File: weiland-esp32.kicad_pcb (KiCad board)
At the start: 2 copper layers, 20.2 x 58 mm, 22 parts, among them J1 S02B-PASK-2, J2 20021221-00006T4LF, J3 S02B-PASK-2, J4 S02B-PASK-2, J6 S02B-PASK-2, J7 S02B-PASK-2, U1 ESP32-WROOM-32E(8MB), U2 AMS1117-3.3_C347222, U3 GR6205-SOP-8, U4 MAX98357AEWL_T

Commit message: good schematic before unshrouded header
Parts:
- removed J3, J4: S02B-PASK-2, footprints:CONN2_S02B-PASK-2_JST
- removed U3: GR6205-SOP-8, motor_driver:SOP127P780X200-8N
- added P1: S04B-PASK-2_LF__SN_, S04B-PASK-2_LF__SN_:JST_S04B-PASK-2, F.Cu at (138.4, 99.9)
- added P2: S04B-PASK-2_LF__SN_, S04B-PASK-2_LF__SN_:JST_S04B-PASK-2, F.Cu at (172.8, 93.5)
- added U5: ULN2003F12FN-7, ULN2003:U-DFN3030-10_DIO, F.Cu at (171.5, 101.4)
- C1: footprint 22uF capacitor:CAPC1608X90N -> 100ohm-resistor:RESC1005X40N
- C4, C5: value 10uF -> 22uF; footprint 10 uF capacitor:CAPC1608X90N -> 100ohm-resistor:RESC1005X40N
- C6: footprint 10 uF capacitor:CAPC1608X90N -> 100ohm-resistor:RESC1005X40N
- C7, C8: footprint 220pF capacitor:CAPC1005X55N -> 100ohm-resistor:RESC1005X40N
- R1: value 5.1kΩ -> 100Ω; footprint 5-1-ohm-resistor:RES_ERJ2RKF5101X -> 100ohm-resistor:RESC1005X40N
- U4: footprint MAX98357AEWL_T:BGA9N40P3X3_134X143X69N -> MAX98357AETE_T:QFN50P300X300X80-17N
- moved J7 42.5 mm to (173.0, 108.1), turned to -90 degrees
- moved J2 33.5 mm to (177.4, 102.2), turned to 0 degrees
- moved J6 28.1 mm to (138.4, 92.3), turned to 90 degrees
- moved C3 27.8 mm to (172.5, 105.1), turned to 0 degrees
- moved U1 24.0 mm to (159.1, 96.1), turned to 0 degrees
- moved C5 22.7 mm to (147.6, 99.8)
- moved C4 21.1 mm to (144.1, 99.8), turned to 180 degrees
- moved U2 20.2 mm to (145.7, 94.6), turned to -90 degrees
- moved C2 20.2 mm to (146.5, 89.5)
- moved C1 20.0 mm to (143.8, 89.5)
- moved R1 17.0 mm to (147.9, 101.3), turned to 0 degrees
- moved LED1 13.6 mm to (145.1, 101.4), turned to 180 degrees
- moved J1 12.3 mm to (138.4, 109.4), turned to 90 degrees
- moved C6 10.8 mm to (143.3, 104.1), turned to -90 degrees
- moved U4 7.80 mm to (146.7, 104.8)
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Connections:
- U1 pad 10: /IO25 -> unconnected-(U1-IO25-Pad10)
- U1 pad 11: /IO26 -> unconnected-(U1-IO26-Pad11)
- U1 pad 12: /IO27 -> unconnected-(U1-IO27-Pad12)
- U1 pad 13: unconnected-(U1-IO14-Pad13) -> /IO14
- U1 pad 23: unconnected-(U1-IO15-Pad23) -> /IO15
- U1 pad 27: unconnected-(U1-IO16-Pad27) -> /IO16
- U1 pad 28: unconnected-(U1-IO17-Pad28) -> /IO17
- U1 pad 30: unconnected-(U1-IO18-Pad30) -> /IO18
- U1 pad 31: unconnected-(U1-IO19-Pad31) -> /IO19
- U1 pad 36: unconnected-(U1-IO22-Pad36) -> /IO22
- U1 pad 8: /IO32 -> unconnected-(U1-IO32-Pad8)
- U1 pad 9: /IO33 -> unconnected-(U1-IO33-Pad9)
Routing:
- net GND: track 104.8 -> 1.40 mm, vias 4 -> 2
- net /OUTN: track 46.2 -> 0.00 mm, vias 6 -> 0
- net /OUTP: track 44.6 -> 0.00 mm, vias 2 -> 0
- net /RXD0: track 32.6 -> 0.00 mm, vias 2 -> 0
- net /TXD0: track 32.5 -> 0.00 mm, vias 2 -> 0
- net +5V: track 32.4 -> 62.2 mm, vias 2 -> 1
- net /IO0: track 26.6 -> 0.00 mm, vias 2 -> 0
- net /OUTA: track 31.6 -> 7.37 mm
- net /EN: track 22.5 -> 0.00 mm, vias 2 -> 0
- net /IO25: track 20.6 -> 0.00 mm
- net /IO26: track 13.1 -> 0.00 mm, vias 2 -> 0
- net /IO27: track 13.0 -> 0.00 mm, vias 2 -> 0
- net +3V3: track 21.4 -> 13.7 mm, vias 2 -> 0
- net Net-(U4-OUTN): track 3.06 -> 0.00 mm
- net /IO33: track 2.58 -> 0.00 mm
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- added copper zone on B.Cu, net GND
- added copper zone on F.Cu, net GND
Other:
- board size 20.2 x 58 mm -> 51.5 x 24.2 mm

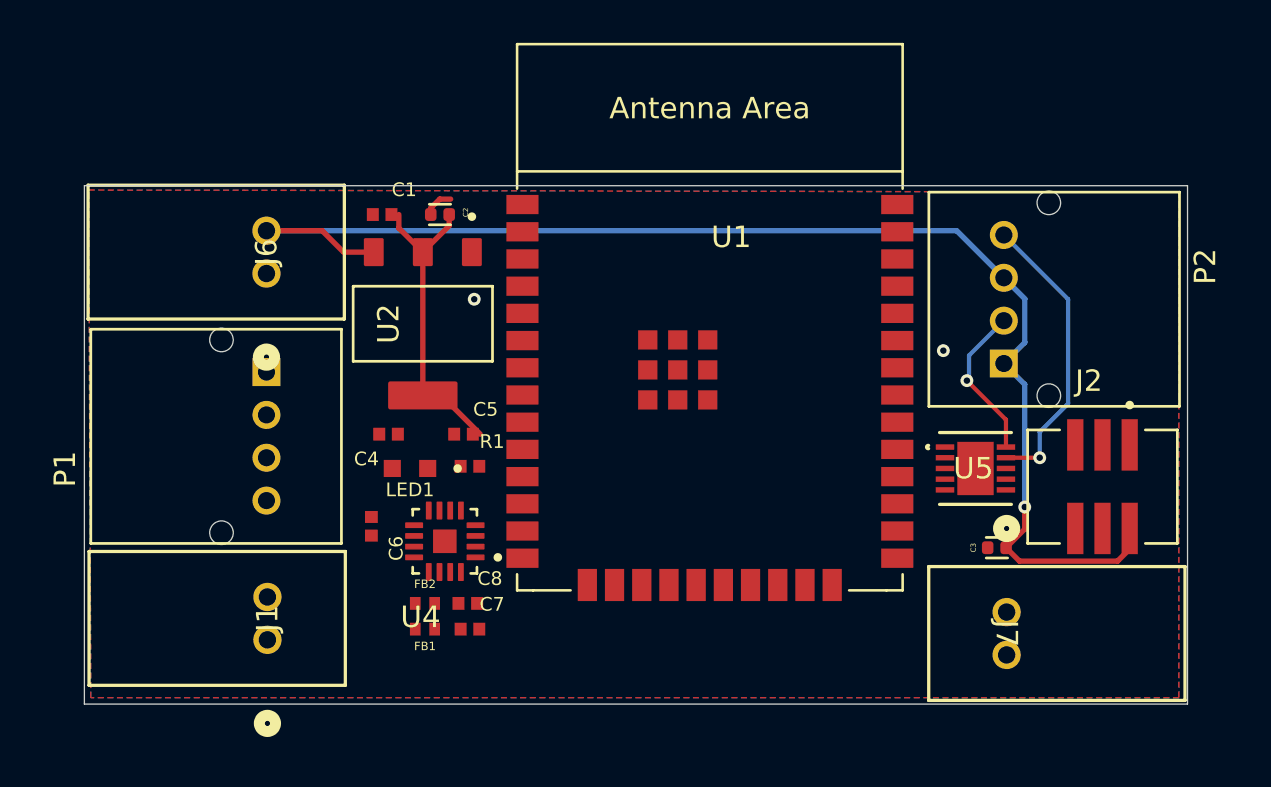
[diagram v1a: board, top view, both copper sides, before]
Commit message: test point schematic, before adding to layout
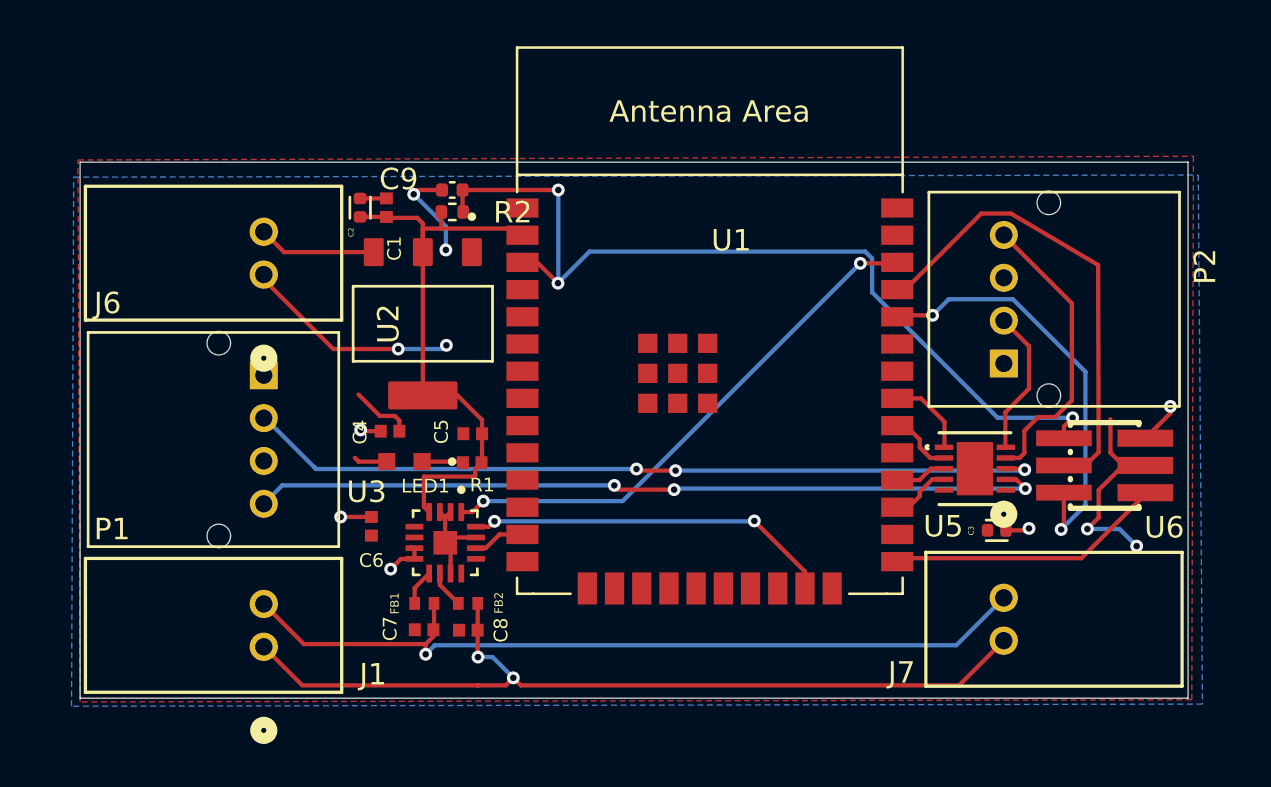
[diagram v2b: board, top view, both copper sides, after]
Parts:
- removed J2: 20021221-00006T4LF, dc3-6p:dc3-6p
- removed U4: MAX98357AEWL_T, MAX98357AETE_T:QFN50P300X300X80-17N
- added C9: 0.1uF, Capacitor_SMD:C_0402_1005Metric, F.Cu at (147.1, 88.4)
- added R2: 10k, Resistor_SMD:R_0402_1005Metric, F.Cu at (147.1, 89.4)
- added U3: MAX98357AETE_T, MAX98357AETE_T:QFN50P300X300X80-17N, F.Cu at (146.7, 104.9)
- added U6: DZ127S-22-06-55, unshroudedheader:HDR-SMD_6P-P1.27-V-M-R2-C3-S1.27-LS5.5-1, F.Cu at (177.5, 101.3)
- moved C2 3.74 mm to (142.8, 89.2), turned to -90 degrees
- moved C7 2.14 mm to (145.8, 108.9), turned to 180 degrees
- moved FB2 2.01 mm to (147.8, 107.7)
- moved C8 1.25 mm to (147.8, 109.0), turned to 180 degrees
- moved FB1 1.20 mm to (145.8, 107.7)
- moved C3 0.81 mm to (172.5, 104.3)
- moved J7 0.68 mm to (172.8, 107.4)
- moved C5 0.43 mm to (148.0, 99.8)
- moved LED1 0.41 mm to (144.8, 101.1)
- moved C1 0.38 mm to (144.0, 89.2), turned to -90 degrees
- moved J1 0.37 mm to (138.3, 109.7)
- moved R1 0.20 mm to (148.0, 101.1)
- moved P1 0.20 mm to (138.3, 100.0)
- moved U1 0.16 mm to (159.1, 96.2)
- moved C4 0.16 mm to (144.2, 99.7)
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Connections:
- net +3V3 renamed +3.3V
- J1 pad 1: /OUTP -> /OUTN
- J1 pad 2: /OUTN -> /OUTP
- P1 pad 2: /OUTD -> /OUTC
- P1 pad 4: /OUTC -> /OUTD
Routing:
- net +5V: track 62.2 -> 12.9 mm, vias 1 -> 5
- net /EN: track 0.00 -> 41.8 mm, vias 0 -> 3
- net /OUTN: track 0.00 -> 41.1 mm, vias 0 -> 2
- net /OUTP: track 0.00 -> 38.9 mm, vias 0 -> 1
- net /OUTC: track 0.00 -> 37.5 mm, vias 0 -> 3
- net /OUTD: track 0.00 -> 37.1 mm, vias 0 -> 3
- net GND: track 1.40 -> 35.2 mm, vias 2 -> 6
- net /IO22: track 0.00 -> 25.2 mm, vias 0 -> 2
- net /TXD0: track 0.00 -> 22.1 mm
- net /RXD0: track 0.00 -> 20.1 mm, vias 0 -> 2
- net /IO15: track 0.00 -> 17.2 mm, vias 0 -> 2
- net +3.3V: track 13.7 -> 28.0 mm
- net /IO0: track 0.00 -> 13.0 mm
- net /IO19: track 0.00 -> 3.84 mm
- net /IO18: track 0.00 -> 3.04 mm
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- added copper zone on B.Cu, net +5V
- removed copper zone on B.Cu, net GND
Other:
- board size 51.5 x 24.2 mm -> 51.7 x 25 mm

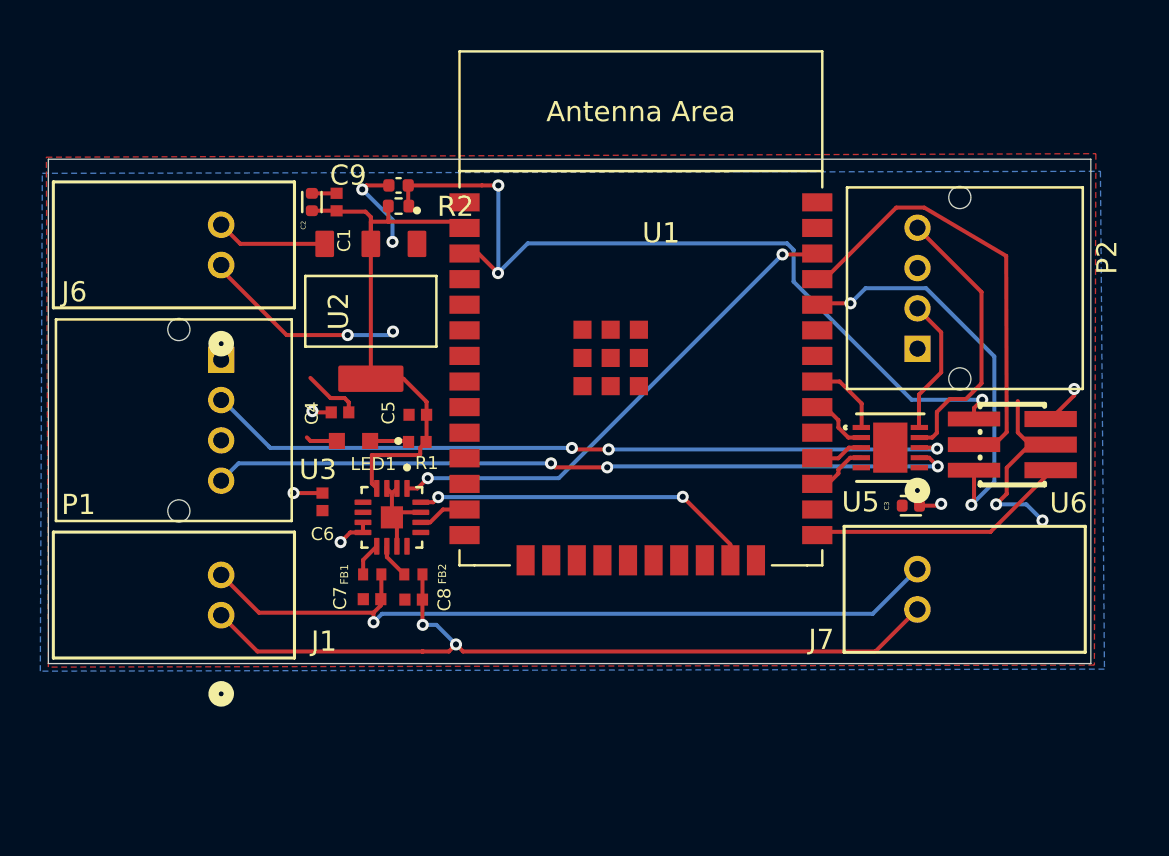
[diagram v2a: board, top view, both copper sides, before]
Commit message: 52x39 board w/ holes
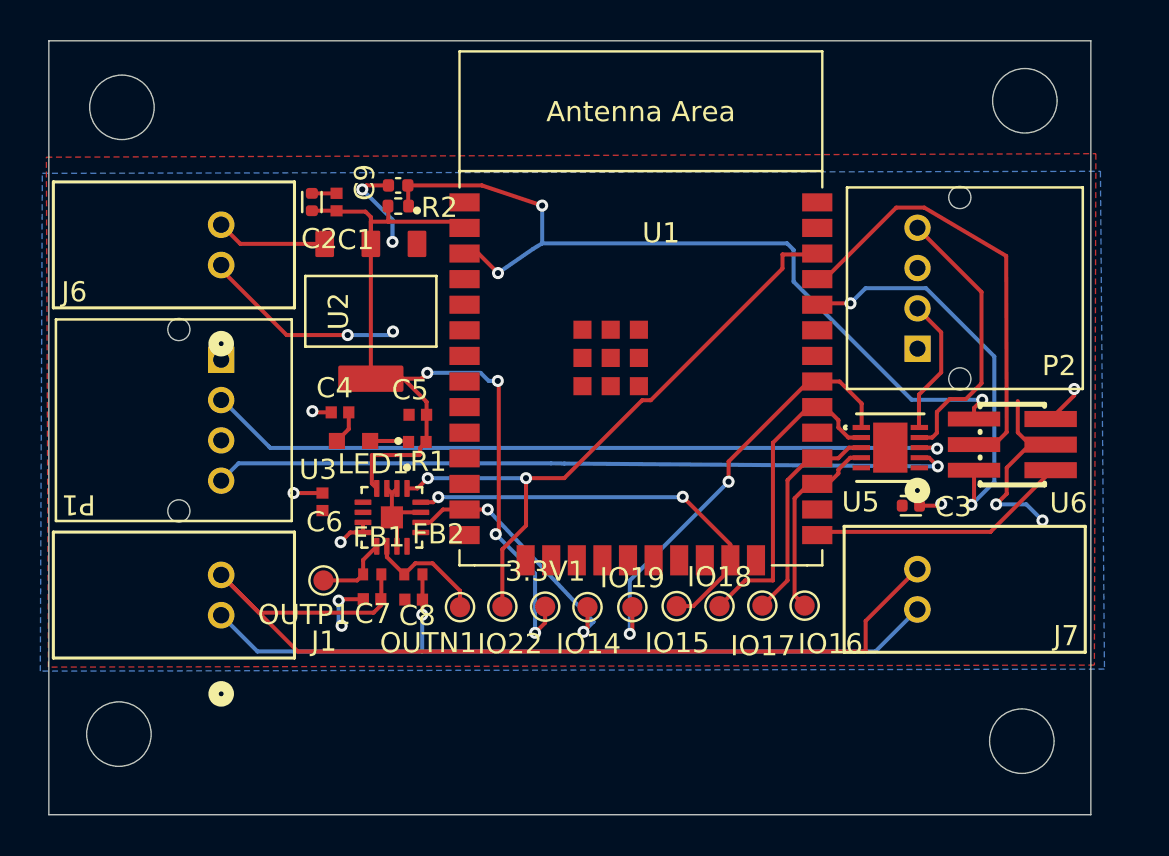
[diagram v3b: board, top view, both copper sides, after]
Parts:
- added 3.3V1: TestPoint, TestPoint:TestPoint_Pad_D1.0mm, F.Cu at (154.3, 109.3)
- added IO14: TestPoint, TestPoint:TestPoint_Pad_D1.0mm, F.Cu at (156.4, 109.3)
- added IO15: TestPoint, TestPoint:TestPoint_Pad_D1.0mm, F.Cu at (160.9, 109.3)
- added IO16: TestPoint, TestPoint:TestPoint_Pad_D1.0mm, F.Cu at (167.2, 109.2)
- added IO17: TestPoint, TestPoint:TestPoint_Pad_D1.0mm, F.Cu at (165.1, 109.2)
- added IO18: TestPoint, TestPoint:TestPoint_Pad_D1.0mm, F.Cu at (163.0, 109.3)
- added IO19: TestPoint, TestPoint:TestPoint_Pad_D1.0mm, F.Cu at (158.7, 109.3)
- added IO22: TestPoint, TestPoint:TestPoint_Pad_D1.0mm, F.Cu at (152.2, 109.3)
- added OUTN1: TestPoint, TestPoint:TestPoint_Pad_D1.0mm, F.Cu at (150.1, 109.3)
- added OUTP1: TestPoint, TestPoint:TestPoint_Pad_D1.0mm, F.Cu at (143.3, 108.0)
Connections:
- net Net-(U3-OUTN) renamed /PRE-OUTN
- net Net-(U3-OUTP) renamed /PRE-OUTP
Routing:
- net +3.3V: track 28.0 -> 49.5 mm, vias 0 -> 4
- net /IO19: track 3.84 -> 21.8 mm, vias 0 -> 2
- net /IO18: track 3.04 -> 16.0 mm
- net /IO14: track 2.44 -> 13.3 mm, vias 0 -> 2
- net /OUTP: track 38.9 -> 49.1 mm, vias 1 -> 0
- net /IO17: track 2.42 -> 11.1 mm
- net /IO22: track 25.2 -> 32.5 mm
- net /IO16: track 2.85 -> 9.81 mm
- net /PRE-OUTN: track 1.75 -> 6.12 mm
- net /IO15: track 17.2 -> 21.1 mm
- net /PRE-OUTP: track 1.68 -> 3.77 mm
- net /OUTN: track 41.1 -> 40.0 mm, vias 2 -> 1
- net GND: track 35.2 -> 34.9 mm, vias 6 -> 8
- net /OUTD: track 37.1 -> 37.0 mm, vias 3 -> 1
- net /OUTC: vias 3 -> 1
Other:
- board size 51.7 x 25 mm -> 51.7 x 38.4 mm

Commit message: before deleting all traces
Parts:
- added H1: MountingHole, MountingHole:MountingHole_3.2mm_M3, F.Cu at (137.7, 108.3)
- added H2: MountingHole, MountingHole:MountingHole_3.2mm_M3, F.Cu at (175.0, 119.1)
- moved J1 8.60 mm to (129.7, 109.6)
- moved J6 8.60 mm to (129.7, 92.2)
- moved P1 8.60 mm to (129.7, 100.0)
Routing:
- net /OUTP: track 49.1 -> 67.4 mm
- net +5V: track 12.9 -> 21.6 mm
- net /OUTN: track 40.0 -> 48.6 mm
- net /OUTC: track 37.5 -> 46.1 mm
- net /OUTD: track 37.0 -> 45.6 mm
- net GND: track 34.9 -> 43.5 mm
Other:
- board size 51.7 x 38.4 mm -> 70.8 x 24.6 mm

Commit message: board complete
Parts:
- added H3: MountingHole, MountingHole:MountingHole_3.2mm_M3, F.Cu at (172.4, 108.4)
- added H4: MountingHole, MountingHole:MountingHole_3.2mm_M3, F.Cu at (145.7, 91.4)
- moved P+1 33.1 mm to (174.7, 97.4)
- moved C9 30.1 mm to (177.1, 90.5)
- moved R2 30.1 mm to (177.1, 91.5)
- moved FB1 29.4 mm to (173.9, 99.4), turned to -90 degrees
- moved C7 28.9 mm to (174.2, 104.1), turned to -90 degrees
- moved FB2 28.5 mm to (175.1, 99.4), turned to -90 degrees
- moved C6 28.4 mm to (171.3, 99.7), turned to 180 degrees
- moved N1 28.2 mm to (174.7, 95.3)
- moved C8 28.0 mm to (175.4, 104.1), turned to -90 degrees
- moved H2 27.9 mm to (172.4, 91.3)
- moved U3 25.6 mm to (171.1, 97.0), turned to 0 degrees
- moved C3 19.0 mm to (185.9, 90.8), turned to 90 degrees
- moved C2 16.2 mm to (142.8, 105.4), turned to 90 degrees
- moved I22 14.3 mm to (166.5, 109.2)
- moved U6 10.7 mm to (182.0, 91.6)
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- renumbered IO14 to I14, IO15 to I15, IO16 to I16, IO17 to I17, IO18 to I18, IO19 to I19, IO22 to I22, OUTN1 to N1, OUTP1 to P+1, 3.3V1 to V3
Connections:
- P2 pad 2: /OUTA -> /OUTB
- P2 pad 4: /OUTB -> /OUTA
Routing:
- net +3.3V: track 49.5 -> 83.5 mm, vias 4 -> 8
- net GND: track 43.5 -> 22.3 mm, vias 8 -> 4
- net /IO14: track 13.3 -> 34.1 mm
- net /IO0: track 13.0 -> 27.0 mm, vias 0 -> 2
- net Net-(LED1-A): track 1.93 -> 14.0 mm
- net /OUTP: track 67.4 -> 56.8 mm, vias 0 -> 1
- net /OUTD: track 45.6 -> 36.5 mm
- net +5V: track 21.6 -> 12.7 mm, vias 5 -> 2
- net /TXD0: track 22.1 -> 13.5 mm, vias 0 -> 2
- net /OUTC: track 46.1 -> 37.6 mm
- net /EN: track 41.5 -> 33.4 mm, vias 3 -> 0
- net /OUTN: track 48.6 -> 56.0 mm
- net /RXD0: track 20.1 -> 12.9 mm
- net /OUTB: track 13.8 -> 7.35 mm, vias 0 -> 1
- net /IO17: track 11.1 -> 17.5 mm, vias 0 -> 4
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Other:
- board size 70.8 x 24.6 mm -> 58.5 x 24.2 mm

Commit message: test
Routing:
- removed copper zone on B.Cu, net +5V
- removed copper zone on F.Cu, net GND
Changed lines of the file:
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@@
 		)
 		(property "Value" "10uF"
-			(at 3.8768 1.0936 360)
+			(at 3.8768 1.0936 0)
 			(layer "F.Fab")
 			(effects
@@
 		)
 		(property "Footprint" "100ohm-resistor:RESC1005X40N"
-			(at 0 0 360)
+			(at 0 0 0)
 			(layer "F.Fab")
 			(hide yes)
@@
 		)
 		(property "Datasheet" ""
-			(at 0 0 360)
+			(at 0 0 0)
 			(layer "F.Fab")
 			(hide yes)
@@
 		)
 		(property "Description" "Unpolarized capacitor"
-			(at 0 0 360)
+			(at 0 0 0)
 			(layer "F.Fab")
 			(hide yes)
@@
 		)
 		(property "Value" "22uF"
-			(at 3.8768 1.0936 360)
+			(at 3.8768 1.0936 0)
 			(layer "F.Fab")
 			(effects
@@
 		)
 		(property "Footprint" "100ohm-resistor:RESC1005X40N"
-			(at 0 0 360)
+			(at 0 0 0)
 			(layer "F.Fab")
 			(hide yes)
@@
 		)
 		(property "Datasheet" ""
-			(at 0 0 360)
+			(at 0 0 0)
 			(layer "F.Fab")
 			(hide yes)
@@
 		)
 		(property "Description" ""
-			(at 0 0 360)
+			(at 0 0 0)
 			(layer "F.Fab")
 			(hide yes)
@@
 		)
 		(property "LCSC" "C22367823"
-			(at 0 0 360)
+			(at 0 0 0)
 			(layer "F.SilkS")
 			(hide yes)
@@
 		)
 		(property "Value" "0.1uF"
-			(at 0 1.16 360)
+			(at 0 1.16 0)
 			(layer "F.Fab")
 			(effects
@@
 		)
 		(fp_text user "${REFERENCE}"
-			(at 0 0 360)
+			(at 0 0 0)
 			(layer "F.Fab")
 			(effects
@@
 		)
 		(property "Value" "22uF"
-			(at 3.8768 1.0936 360)
+			(at 3.8768 1.0936 0)
 			(layer "F.Fab")
 			(effects
@@
 		)
 		(property "Footprint" "100ohm-resistor:RESC1005X40N"
-			(at 0 0 360)
+			(at 0 0 0)
 			(layer "F.Fab")
 			(hide yes)
@@
 		)
 		(property "Datasheet" ""
-			(at 0 0 360)
+			(at 0 0 0)
 			(layer "F.Fab")
 			(hide yes)
@@
 		)
 		(property "Description" ""
-			(at 0 0 360)
+			(at 0 0 0)
 			(layer "F.Fab")
 			(hide yes)
@@
 		)
 		(property "LCSC" "C22367823"
-			(at 0 0 360)
+			(at 0 0 0)
 			(layer "F.SilkS")
 			(hide yes)
@@
 		)
 		(property "Value" "10k"
-			(at 0 1.17 360)
+			(at 0 1.17 0)
 			(layer "F.Fab")
 			(effects
@@
 		)
 		(fp_text user "${REFERENCE}"
-			(at 0 0 360)
+			(at 0 0 0)
 			(layer "F.Fab")
 			(effects
@@
 		)
 		(property "Value" "MAX98357AETE_T"
-			(at 10.36 3.74 360)
+			(at 10.36 3.74 0)
 			(layer "F.Fab")
 			(effects
@@
 		)
 		(property "Footprint" "MAX98357AETE_T:QFN50P300X300X80-17N"
-			(at 0 0 360)
+			(at 0 0 0)
 			(layer "F.Fab")
 			(hide yes)
@@
 		)
 		(property "Datasheet" ""
-			(at 0 0 360)
+			(at 0 0 0)
 			(layer "F.Fab")
 			(hide yes)
@@
 		)
 		(property "Description" ""
-			(at 0 0 360)
+			(at 0 0 0)
 			(layer "F.Fab")
 			(hide yes)
@@
 		(net 47)
 	)
-	(zone
-		(net 1)
-		(net_name "GND")
-		(layer "F.Cu")
-		(hatch edge 0.5)
-		(connect_pads
-			(clearance 0.2)
-		)
-		(min_thickness 0.25)
-		(filled_areas_thickness no)
-		(fill yes
-			(thermal_gap 0.5)
-			(thermal_bridge_width 0.5)
-		)
-		(polygon
-			(pts
-				(xy 129.5 87.5) (xy 188.6 87.6) (xy 188.85 113.075) (xy 128.775 113.45)
-			)
-		)
-	)
-	(zone
-		(net 2)
-		(net_name "+5V")
-		(layer "B.Cu")
-		(hatch edge 0.5)
-		(priority 1)
-		(connect_pads
-			(clearance 0.2)
-		)
-		(min_thickness 0.25)
-		(filled_areas_thickness no)
-		(fill yes
-			(thermal_gap 0.5)
-			(thermal_bridge_width 0.5)
-		)
-		(polygon
-			(pts
-				(xy 129.05 86.925) (xy 188.75 86.925) (xy 189.025 114) (xy 128.15 113.7) (xy 129.05 86.95)
-			)
-		)
-	)
 )
